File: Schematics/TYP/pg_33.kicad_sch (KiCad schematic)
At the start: 12 parts, among them U3501 F280, U3502 F280, U3503 F280, U3504 F280, U3505 F280, U3506 F280, U3507 F280, U3508 F280, U3509 F240, U3510 F240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

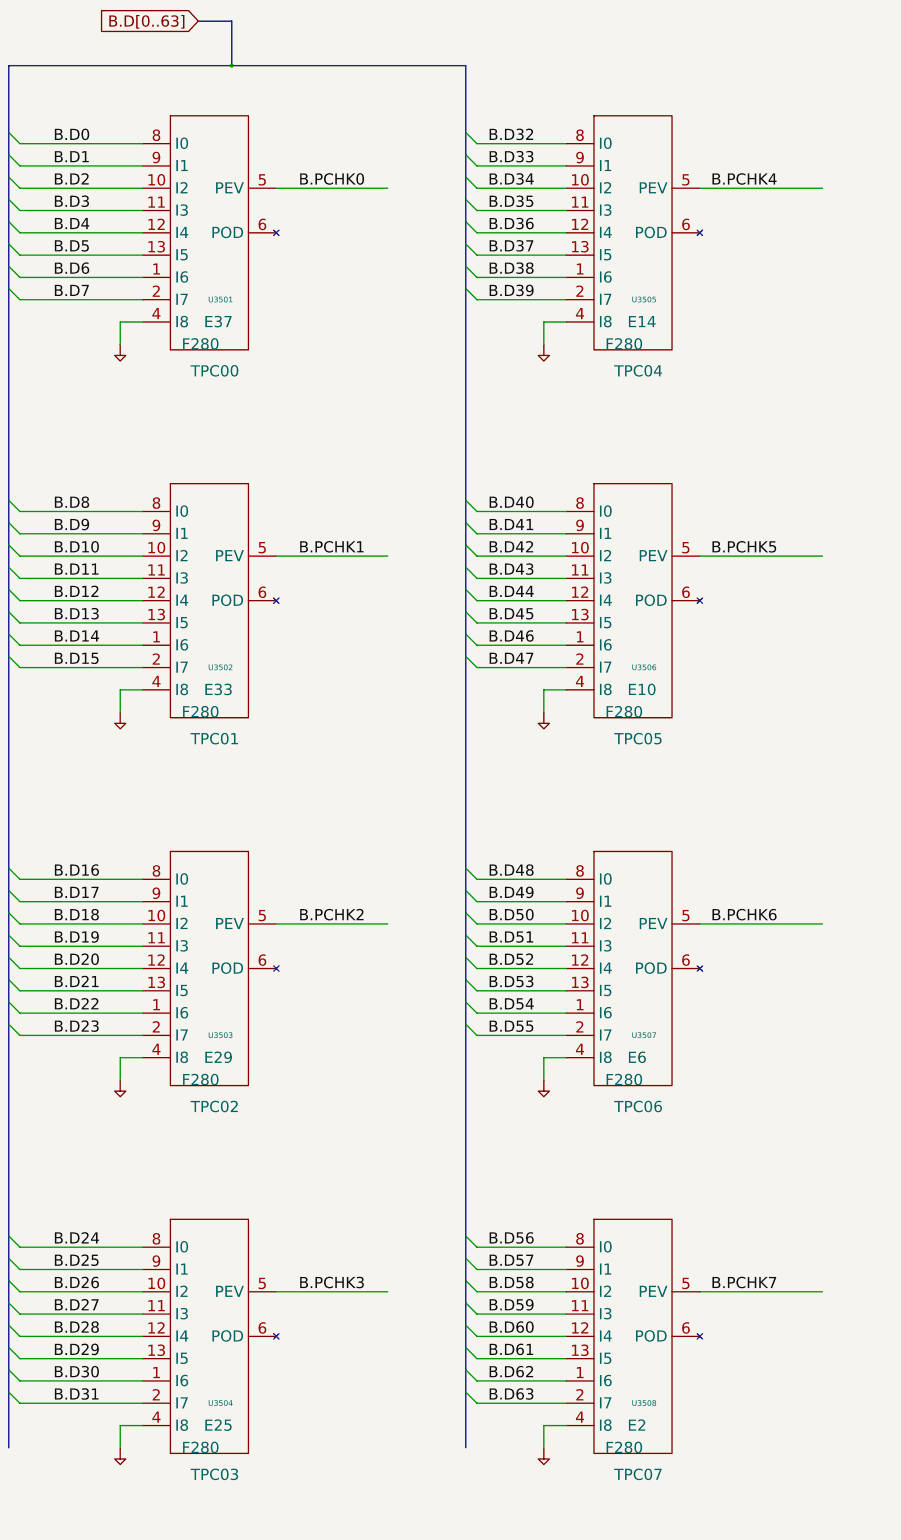
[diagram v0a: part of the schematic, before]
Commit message: Use XSR16 for UEVNT
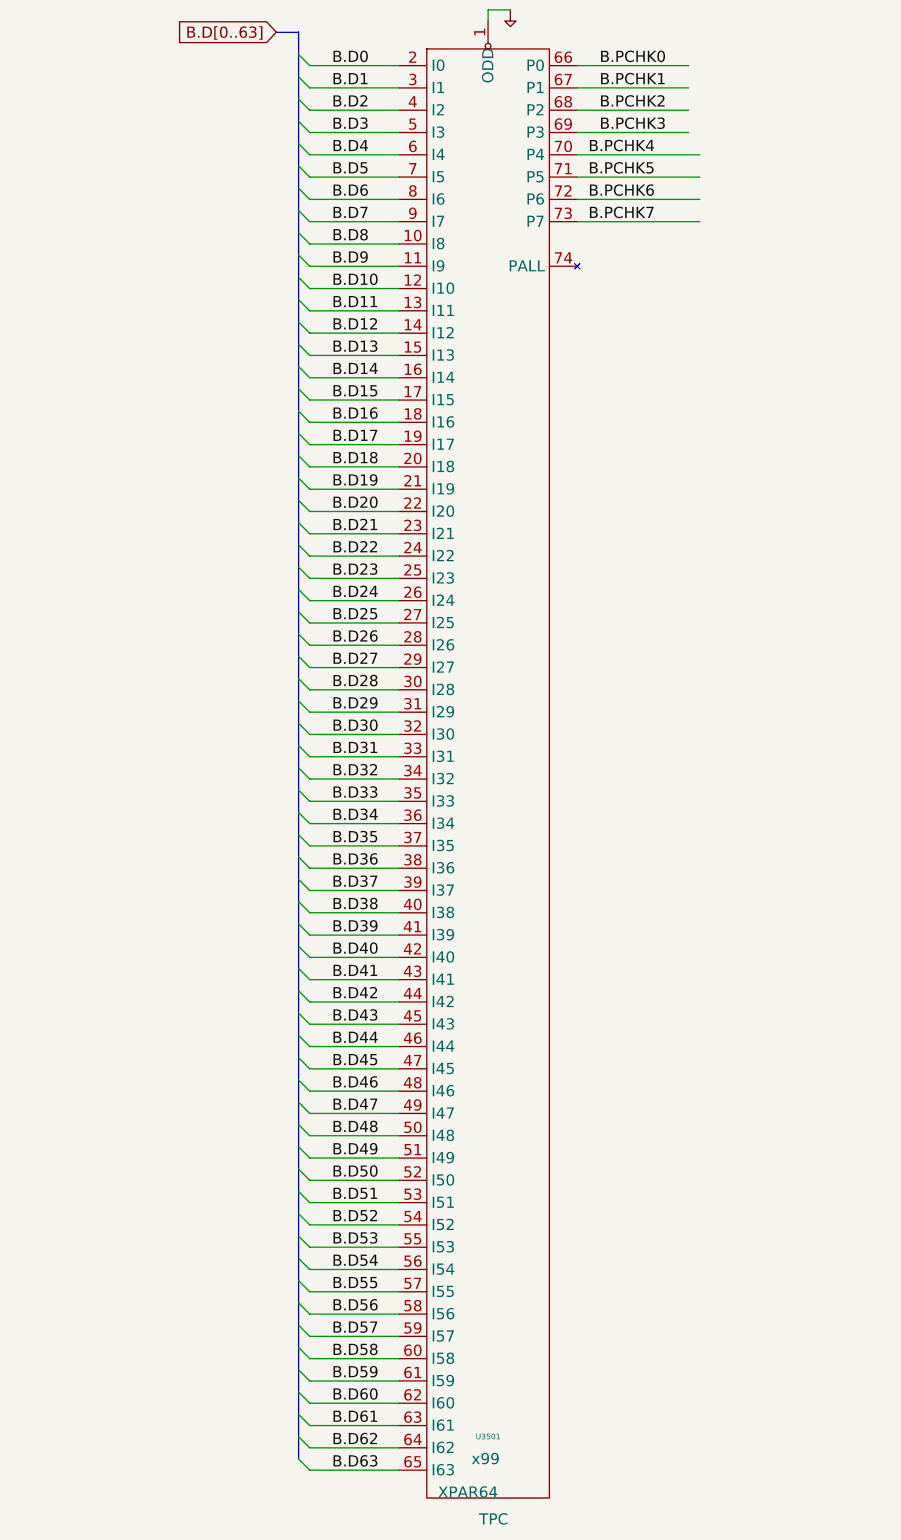
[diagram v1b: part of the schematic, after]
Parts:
- removed U3502, U3503, U3504, U3505, U3506, U3507, U3508: F280, symbol r1000:F280
- U3501: value F280 -> XPAR64; symbol r1000:F280 -> r1000:XPAR64; Location E37 -> x99; Name TPC00 -> TPC
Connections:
- net B.D0: now also U3501.2 (I0); no longer U3501.8 (I0)
- net B.D1: now also U3501.3 (I1); no longer U3501.9 (I1)
- net B.D10: now also U3501.12 (I10)
- net B.D11: now also U3501.13 (I11)
- net B.D12: now also U3501.14 (I12)
- net B.D13: now also U3501.15 (I13)
- net B.D14: now also U3501.16 (I14)
- net B.D15: now also U3501.17 (I15)
- net B.D16: now also U3501.18 (I16)
- net B.D17: now also U3501.19 (I17)
- net B.D18: now also U3501.20 (I18)
- net B.D19: now also U3501.21 (I19)
- net B.D2: now also U3501.4 (I2); no longer U3501.10 (I2)
- net B.D20: now also U3501.22 (I20)
- net B.D21: now also U3501.23 (I21)
- net B.D22: now also U3501.24 (I22)
- net B.D23: now also U3501.25 (I23)
- net B.D24: now also U3501.26 (I24)
- net B.D25: now also U3501.27 (I25)
- net B.D26: now also U3501.28 (I26)
- net B.D27: now also U3501.29 (I27)
- net B.D28: now also U3501.30 (I28)
- net B.D29: now also U3501.31 (I29)
- net B.D3: now also U3501.5 (I3); no longer U3501.11 (I3)
- net B.D30: now also U3501.32 (I30)
- net B.D31: now also U3501.33 (I31)
- net B.D32: now also U3501.34 (I32)
- net B.D33: now also U3501.35 (I33)
- net B.D34: now also U3501.36 (I34)
- net B.D35: now also U3501.37 (I35)
- net B.D36: now also U3501.38 (I36)
- net B.D37: now also U3501.39 (I37)
- net B.D38: now also U3501.40 (I38)
- net B.D39: now also U3501.41 (I39)
- net B.D4: now also U3501.6 (I4); no longer U3501.12 (I4)
- net B.D40: now also U3501.42 (I40)
- net B.D41: now also U3501.43 (I41)
- net B.D42: now also U3501.44 (I42)
- net B.D43: now also U3501.45 (I43)
- net B.D44: now also U3501.46 (I44)
- net B.D45: now also U3501.47 (I45)
- net B.D46: now also U3501.48 (I46)
- net B.D47: now also U3501.49 (I47)
- net B.D48: now also U3501.50 (I48)
- net B.D49: now also U3501.51 (I49)
- net B.D5: now also U3501.7 (I5); no longer U3501.13 (I5)
- net B.D50: now also U3501.52 (I50)
- net B.D51: now also U3501.53 (I51)
- net B.D52: now also U3501.54 (I52)
- net B.D53: now also U3501.55 (I53)
- net B.D54: now also U3501.56 (I54)
- net B.D55: now also U3501.57 (I55)
- net B.D56: now also U3501.58 (I56)
- net B.D57: now also U3501.59 (I57)
- net B.D58: now also U3501.60 (I58)
- net B.D59: now also U3501.61 (I59)
- net B.D6: now also U3501.8 (I6); no longer U3501.1 (I6)
- net B.D60: now also U3501.62 (I60)
- net B.D61: now also U3501.63 (I61)
- net B.D62: now also U3501.64 (I62)
- net B.D63: now also U3501.65 (I63)
- net B.D7: now also U3501.9 (I7); no longer U3501.2 (I7)
- net B.D8: now also U3501.10 (I8)
- net B.D9: now also U3501.11 (I9)
- net B.PCHK0: now also U3501.66 (P0); no longer U3501.5 (PEV)
- net B.PCHK1: now also U3501.67 (P1)
- net B.PCHK2: now also U3501.68 (P2)
- net B.PCHK3: now also U3501.69 (P3)
- net B.PCHK4: now also U3501.70 (P4)
- net B.PCHK5: now also U3501.71 (P5)
- net B.PCHK6: now also U3501.72 (P6)
- net B.PCHK7: now also U3501.73 (P7)
- net PD: now also U3501.1 (ODD); no longer U3501.4 (I8)
- no-connect marks 8 -> 1

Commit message: Megacomp'ification
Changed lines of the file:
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@@
   (wire (pts (xy 149.86 45.72) (xy 175.26 45.72) ) )
   (wire (pts (xy 149.86 50.8) (xy 175.26 50.8) ) )
-  (wire (pts (xy 149.86 55.88) (xy 177.8 55.88) ) )
-  (wire (pts (xy 149.86 60.96) (xy 177.8 60.96) ) )
-  (wire (pts (xy 149.86 66.04) (xy 177.8 66.04) ) )
-  (wire (pts (xy 149.86 71.12) (xy 177.8 71.12) ) )
+  (wire (pts (xy 149.86 55.88) (xy 175.26 55.88) ) )
+  (wire (pts (xy 149.86 60.96) (xy 175.26 60.96) ) )
+  (wire (pts (xy 149.86 66.04) (xy 175.26 66.04) ) )
+  (wire (pts (xy 149.86 71.12) (xy 175.26 71.12) ) )
   (wire (pts (xy 271.78 200.66) (xy 309.88 200.66) ) )
   (wire (pts (xy 271.78 205.74) (xy 309.88 205.74) ) )
@@
   (symbol (lib_id "r1000:PD") (at 134.62 22.86 0) (unit 1) (in_bom no) (on_board yes) (property "Reference" "#PWR03506" (id 0) (at 134.62 22.86 0) (effects (font (size 1.27 1.27) ) hide ) ) (property "Value" "PD" (id 1) (at 134.62 22.86 0) (effects (font (size 1.27 1.27) ) hide ) ) (property "Footprint" "" (id 2) (at 134.62 22.86 0) (effects (font (size 1.27 1.27) ) hide ) ) (property "Datasheet" "" (id 3) (at 134.62 22.86 0) (effects (font (size 1.27 1.27) ) hide ) ) (pin "1") )
   (no_connect (at 149.86 81.28) )
-  (label "B.PCHK4" (at 152.4 55.88 0) (effects (font (size 2.54 2.54) ) (justify left bottom) ) )
-  (label "B.PCHK5" (at 152.4 60.96 0) (effects (font (size 2.54 2.54) ) (justify left bottom) ) )
-  (label "B.PCHK6" (at 152.4 66.04 0) (effects (font (size 2.54 2.54) ) (justify left bottom) ) )
-  (label "B.PCHK7" (at 152.4 71.12 0) (effects (font (size 2.54 2.54) ) (justify left bottom) ) )
   (label "B.PCHK0" (at 154.94 35.56 0) (effects (font (size 2.54 2.54) ) (justify left bottom) ) )
   (label "B.PCHK1" (at 154.94 40.64 0) (effects (font (size 2.54 2.54) ) (justify left bottom) ) )
   (label "B.PCHK2" (at 154.94 45.72 0) (effects (font (size 2.54 2.54) ) (justify left bottom) ) )
   (label "B.PCHK3" (at 154.94 50.8 0) (effects (font (size 2.54 2.54) ) (justify left bottom) ) )
+  (label "B.PCHK4" (at 154.94 55.88 0) (effects (font (size 2.54 2.54) ) (justify left bottom) ) )
+  (label "B.PCHK5" (at 154.94 60.96 0) (effects (font (size 2.54 2.54) ) (justify left bottom) ) )
+  (label "B.PCHK6" (at 154.94 66.04 0) (effects (font (size 2.54 2.54) ) (justify left bottom) ) )
+  (label "B.PCHK7" (at 154.94 71.12 0) (effects (font (size 2.54 2.54) ) (justify left bottom) ) )
   (global_label "T.TYPE.P[0..7]" (shape input) (at 264.16 193.04 180) (fields_autoplaced) (effects (font (size 2.54 2.54) ) (justify right) ) (property "Intersheet References" "${INTERSHEET_REFS}" (id 0) (at 232.8454 192.8813 0) (effects (font (size 2.54 2.54) ) (justify right) ) ) )
   (bus_entry (at 269.24 198.12) (size 2.54 2.54) )

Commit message: Megacomp'ing TYP
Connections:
- net B.PCHK0: now also U3510.8 (I3); no longer U3509.17 (I7)
- net B.PCHK1: now also U3510.6 (I2); no longer U3509.15 (I6)
- net B.PCHK2: now also U3510.4 (I1); no longer U3509.13 (I5)
- net B.PCHK3: now also U3510.2 (I0); no longer U3509.11 (I4)
- net T.CMPR4: now also U3509.9 (Y4); no longer U3510.18 (Y0)
- net T.CMPR5: now also U3509.7 (Y5); no longer U3510.16 (Y1)
- net T.CMPR6: now also U3509.5 (Y6); no longer U3510.14 (Y2)
- net T.CMPR7: now also U3509.3 (Y7); no longer U3510.12 (Y3)
- net T.TYPE.P0: now also U3510.12 (Y3); no longer U3509.3 (Y7)
- net T.TYPE.P1: now also U3510.14 (Y2); no longer U3509.5 (Y6)
- net T.TYPE.P2: now also U3510.16 (Y1); no longer U3509.7 (Y5)
- net T.TYPE.P3: now also U3510.18 (Y0); no longer U3509.9 (Y4)
- net T.TYPE.P4: now also U3509.11 (I4); no longer U3510.2 (I0)
- net T.TYPE.P5: now also U3509.13 (I5); no longer U3510.4 (I1)
- net T.TYPE.P6: now also U3509.15 (I6); no longer U3510.6 (I2)
- net T.TYPE.P7: now also U3509.17 (I7); no longer U3510.8 (I3)
- net TYPE_DRV.OE~: now also U3510.1 (OE0); no longer U3509.19 (OE1)
- net TYPE_P.OE~: now also U3509.19 (OE1); no longer U3510.1 (OE0)
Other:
- moved on the sheet: U3510, U3511

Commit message: KiCad 6
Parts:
- U3501: value XPAR64 -> (none)
- U3509, U3510: value F240 -> (none)
- U3511: value F244 -> (none)
- U3512: value F521 -> (none)

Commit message: Recover from KiCad-6 munging
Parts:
- U3501: value (none) -> XPAR64
- U3509, U3510: value (none) -> F240
- U3511: value (none) -> F244
- U3512: value (none) -> F521

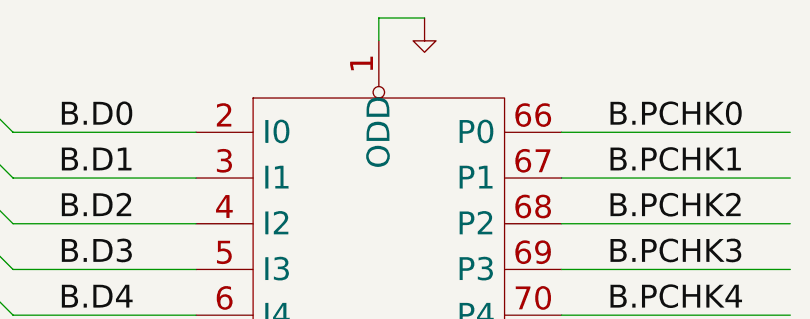
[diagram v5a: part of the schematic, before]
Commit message: Fix XPAR64 parity control
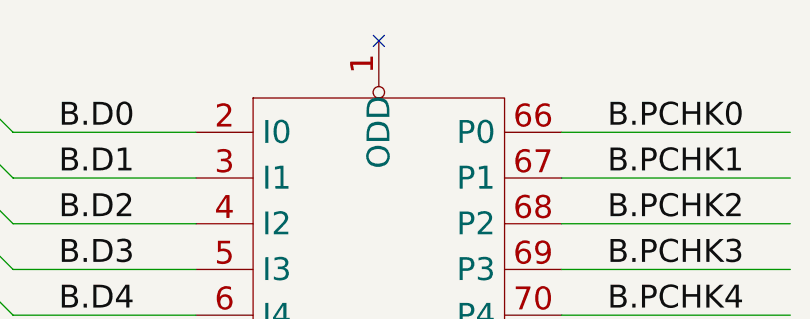
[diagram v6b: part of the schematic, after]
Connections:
- net PD: no longer U3501.1 (ODD)
- no-connect marks 1 -> 2
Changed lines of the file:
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@@
   (bus (pts (xy 86.36 93.98) (xy 86.36 99.06) ) )
   (bus (pts (xy 86.36 99.06) (xy 86.36 104.14) ) )
-  (wire (pts (xy 129.54 22.86) (xy 129.54 25.4) ) )
-  (wire (pts (xy 134.62 22.86) (xy 129.54 22.86) ) )
   (wire (pts (xy 149.86 35.56) (xy 175.26 35.56) ) )
   (wire (pts (xy 149.86 40.64) (xy 175.26 40.64) ) )
@@
   (label "B.D63" (at 93.98 355.6 0) (effects (font (size 2.54 2.54) ) (justify left bottom) ) )
   (symbol (lib_id "r1000:XPAR64") (at 127 353.06 0) (unit 1) (in_bom yes) (on_board yes) (property "Reference" "U3501" (id 0) (at 129.54 347.98 0) (effects (font (size 1.27 1.27) ) ) ) (property "Value" "XPAR64" (id 1) (at 118.11 360.68 0) (effects (font (size 2.54 2.54) ) (justify left) ) ) (property "Footprint" "" (id 2) (at 128.27 354.33 0) (effects (font (size 1.27 1.27) ) hide ) ) (property "Datasheet" "" (id 3) (at 128.27 354.33 0) (effects (font (size 1.27 1.27) ) hide ) ) (property "Location" "x99" (id 4) (at 125.73 353.06 0) (effects (font (size 2.54 2.54) ) (justify left) ) ) (property "Name" "TPC" (id 5) (at 130.81 368.3 0) (effects (font (size 2.54 2.54) ) (justify bottom) ) ) (pin "1") (pin "10") (pin "11") (pin "12") (pin "13") (pin "14") (pin "15") (pin "16") (pin "17") (pin "18") (pin "19") (pin "2") (pin "20") (pin "21") (pin "22") (pin "23") (pin "24") (pin "25") (pin "26") (pin "27") (pin "28") (pin "29") (pin "3") (pin "30") (pin "31") (pin "32") (pin "33") (pin "34") (pin "35") (pin "36") (pin "37") (pin "38") (pin "39") (pin "4") (pin "40") (pin "41") (pin "42") (pin "43") (pin "44") (pin "45") (pin "46") (pin "47") (pin "48") (pin "49") (pin "5") (pin "50") (pin "51") (pin "52") (pin "53") (pin "54") (pin "55") (pin "56") (pin "57") (pin "58") (pin "59") (pin "6") (pin "60") (pin "61") (pin "62") (pin "63") (pin "64") (pin "65") (pin "66") (pin "67") (pin "68") (pin "69") (pin "7") (pin "70") (pin "71") (pin "72") (pin "73") (pin "74") (pin "8") (pin "9") )
-  (symbol (lib_id "r1000:PD") (at 134.62 22.86 0) (unit 1) (in_bom no) (on_board yes) (property "Reference" "#PWR03506" (id 0) (at 134.62 22.86 0) (effects (font (size 1.27 1.27) ) hide ) ) (property "Value" "PD" (id 1) (at 134.62 22.86 0) (effects (font (size 1.27 1.27) ) hide ) ) (property "Footprint" "" (id 2) (at 134.62 22.86 0) (effects (font (size 1.27 1.27) ) hide ) ) (property "Datasheet" "" (id 3) (at 134.62 22.86 0) (effects (font (size 1.27 1.27) ) hide ) ) (pin "1") )
+  (no_connect (at 129.54 25.4) )
   (no_connect (at 149.86 81.28) )
   (label "B.PCHK0" (at 154.94 35.56 0) (effects (font (size 2.54 2.54) ) (justify left bottom) ) )
